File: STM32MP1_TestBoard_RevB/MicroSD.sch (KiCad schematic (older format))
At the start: 6 parts, among them J11 Micro_SD_Card

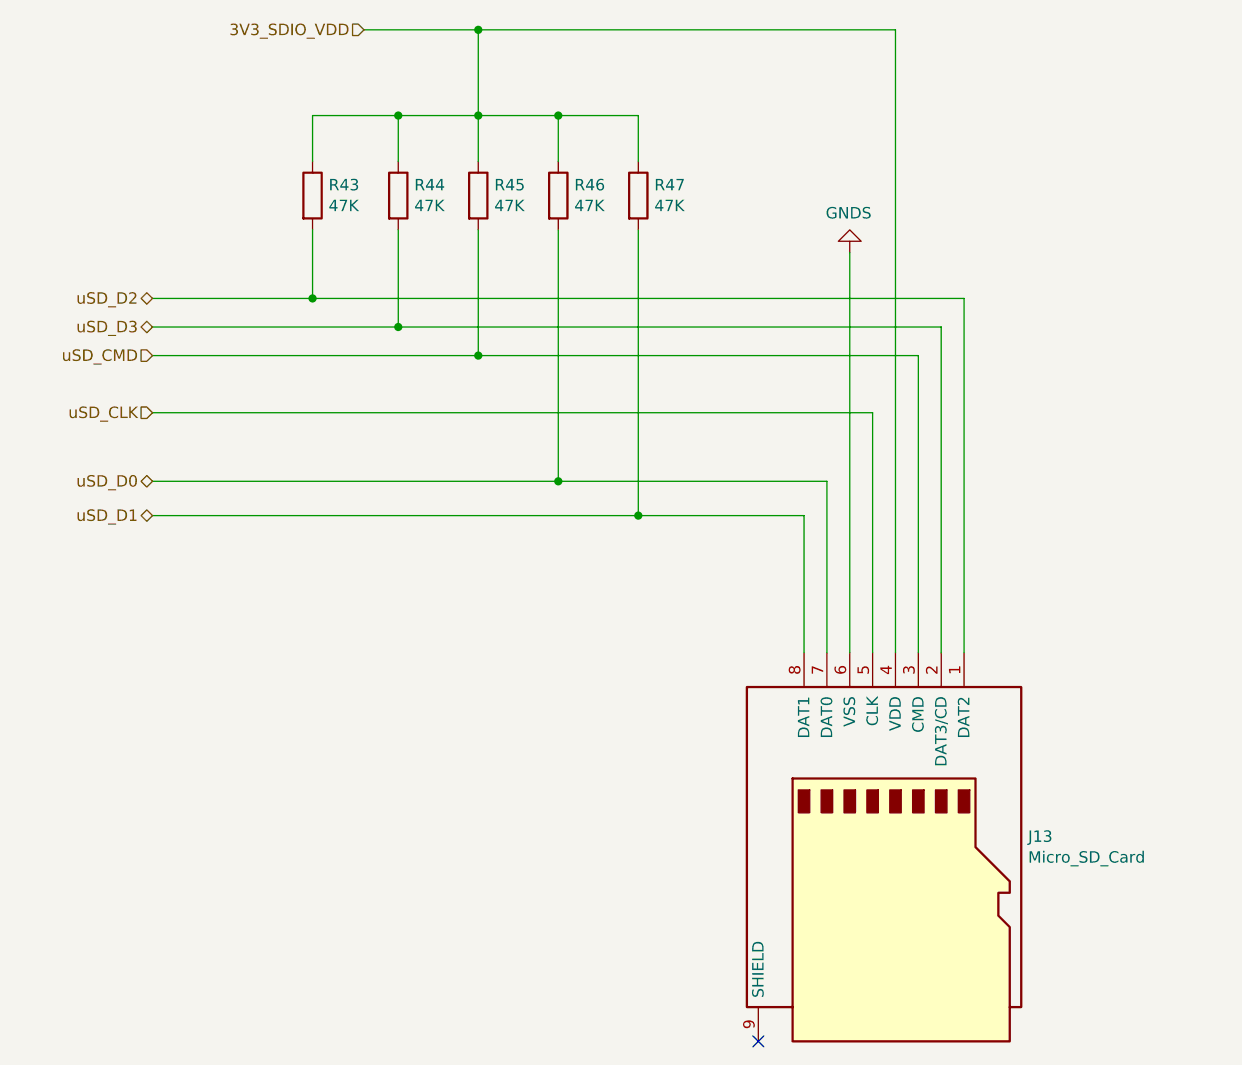
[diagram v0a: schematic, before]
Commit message: Updated design
- Added Crystal/Oscillators
- Replaced both SDMMC with single SDMMC w/ detect pin
- Added USB Type C for VIN
- Moved SWD pins
- Tidied up silk screen for pin headers J1, J2, J3, J4
- Moved DSI socket
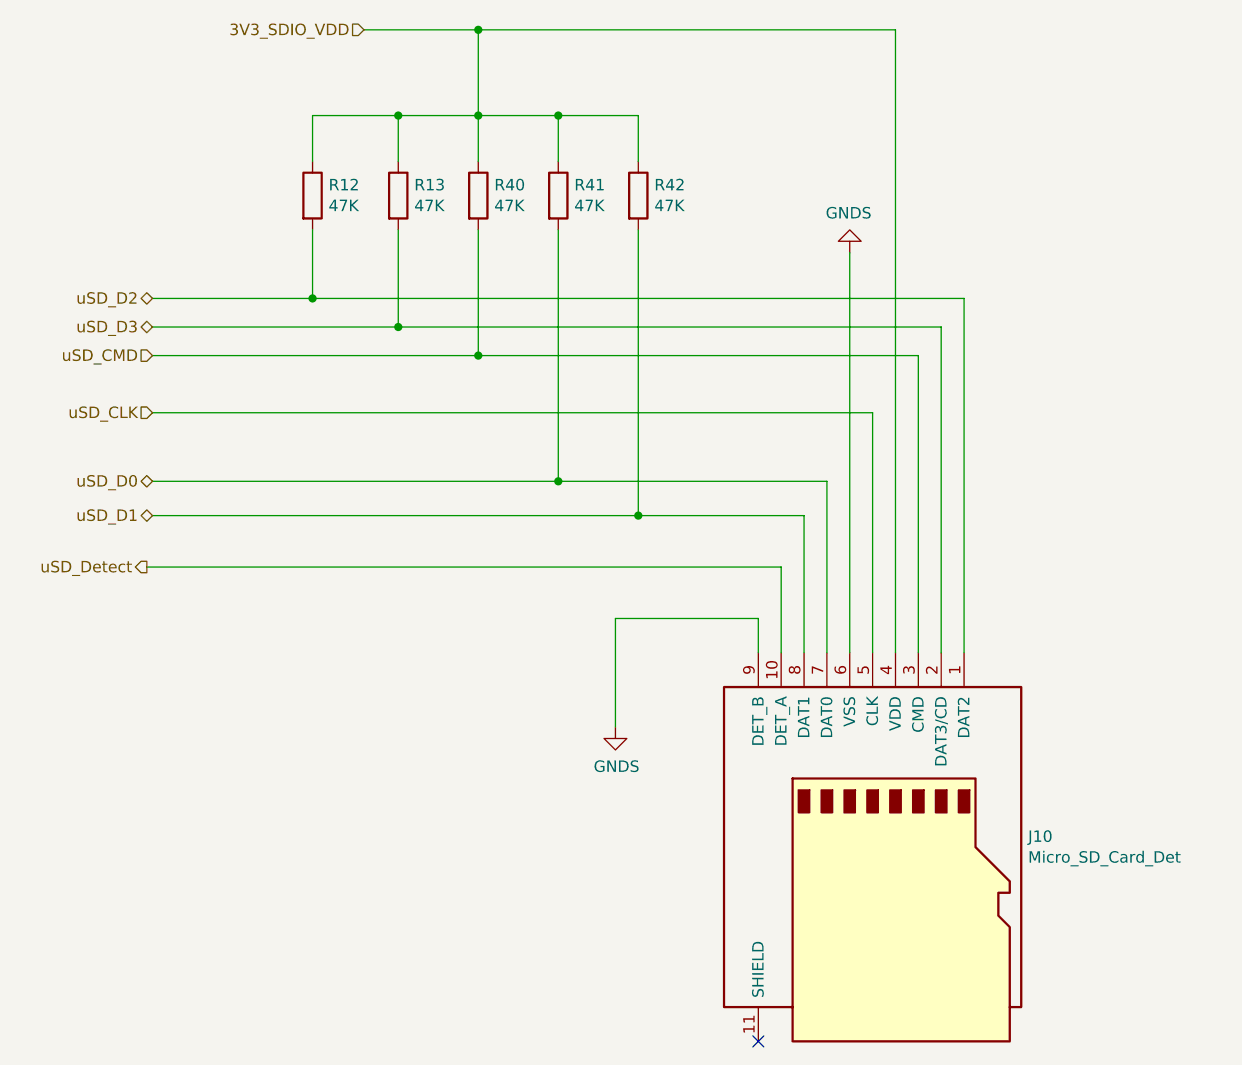
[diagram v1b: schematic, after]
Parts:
- removed J11: Micro_SD_Card, Molex_SDIO:Molex_SDIO_475710001, symbol Connector:Micro_SD_Card
- added J10: Micro_SD_Card_Det, Connector_Card:microSD_HC_Molex_104031-0811, symbol Connector:Micro_SD_Card_Det
- R40, R41, R42, R43, R44: LCSC (none) -> C25792
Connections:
- net 3V3_SDIO_VDD: now also J10.4 (VDD)
- net GNDS: now also J10.6 (VSS), J10.9 (DET_B)
- net uSD_CLK: now also J10.5 (CLK)
- net uSD_CMD: now also J10.3 (CMD)
- net uSD_D0: now also J10.7 (DAT0)
- net uSD_D1: now also J10.8 (DAT1)
- net uSD_D2: now also J10.1 (DAT2)
- net uSD_D3: now also J10.2 (DAT3/CD)
- new net uSD_Detect: J10.10 (DET_A)
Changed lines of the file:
@@
 $Descr A4 11693 8268
 encoding utf-8
-Sheet 10 10
+Sheet 8 9
 Title ""
 Date ""
@@
 AR Path="/6097C138/6099897C/5FB10A8F" Ref="#PWR045"  Part="1"
 AR Path="/6097C138/60E05EB1/5FB10A8F" Ref="#PWR0101"  Part="1"
-F 0 "#PWR0101" H 6900 1725 50  0001 C CNN
+F 0 "#PWR027" H 6900 1725 50  0001 C CNN
 F 1 "GNDS" H 6905 1802 50  0000 C CNN
 F 2 "" H 6900 1975 50  0001 C CNN
@@
 AR Path="/6097C138/6099897C/5FB12D8F" Ref="R43"  Part="1"
 AR Path="/6097C138/60E05EB1/5FB12D8F" Ref="R43"  Part="1"
-F 0 "R43" H 4620 1771 50  0000 L CNN
+F 0 "R12" H 4620 1771 50  0000 L CNN
 F 1 "47K" H 4620 1680 50  0000 L CNN
 F 2 "Resistor_SMD:R_0402_1005Metric_Pad0.72x0.64mm_HandSolder" V 4480 1725 50  0001 C CNN
@@
 F 4 "~" H 4550 1725 50  0001 C CNN "Mfr"
 F 5 "~" H 4550 1725 50  0001 C CNN "PartNo"
+F 6 "C25792" H 4550 1725 50  0001 C CNN "LCSC"
 	1    4550 1725
 	1    0    0    -1
@@
 AR Path="/6097C138/6099897C/5FB155D6" Ref="R44"  Part="1"
 AR Path="/6097C138/60E05EB1/5FB155D6" Ref="R44"  Part="1"
-F 0 "R44" H 4995 1771 50  0000 L CNN
+F 0 "R13" H 4995 1771 50  0000 L CNN
 F 1 "47K" H 4995 1680 50  0000 L CNN
 F 2 "Resistor_SMD:R_0402_1005Metric_Pad0.72x0.64mm_HandSolder" V 4855 1725 50  0001 C CNN
@@
 F 4 "~" H 4925 1725 50  0001 C CNN "Mfr"
 F 5 "~" H 4925 1725 50  0001 C CNN "PartNo"
+F 6 "C25792" H 4925 1725 50  0001 C CNN "LCSC"
 	1    4925 1725
 	1    0    0    -1
@@
 AR Path="/6097C138/6099897C/5FB158C2" Ref="R45"  Part="1"
 AR Path="/6097C138/60E05EB1/5FB158C2" Ref="R45"  Part="1"
-F 0 "R45" H 5345 1771 50  0000 L CNN
+F 0 "R40" H 5345 1771 50  0000 L CNN
 F 1 "47K" H 5345 1680 50  0000 L CNN
 F 2 "Resistor_SMD:R_0402_1005Metric_Pad0.72x0.64mm_HandSolder" V 5205 1725 50  0001 C CNN
@@
 F 4 "~" H 5275 1725 50  0001 C CNN "Mfr"
 F 5 "~" H 5275 1725 50  0001 C CNN "PartNo"
+F 6 "C25792" H 5275 1725 50  0001 C CNN "LCSC"
 	1    5275 1725
 	1    0    0    -1
@@
 AR Path="/6097C138/6099897C/5FB15A9B" Ref="R46"  Part="1"
 AR Path="/6097C138/60E05EB1/5FB15A9B" Ref="R46"  Part="1"
-F 0 "R46" H 5695 1771 50  0000 L CNN
+F 0 "R41" H 5695 1771 50  0000 L CNN
 F 1 "47K" H 5695 1680 50  0000 L CNN
 F 2 "Resistor_SMD:R_0402_1005Metric_Pad0.72x0.64mm_HandSolder" V 5555 1725 50  0001 C CNN
@@
 F 4 "~" H 5625 1725 50  0001 C CNN "Mfr"
 F 5 "~" H 5625 1725 50  0001 C CNN "PartNo"
+F 6 "C25792" H 5625 1725 50  0001 C CNN "LCSC"
 	1    5625 1725
 	1    0    0    -1
@@
 AR Path="/6097C138/6099897C/5FB15D60" Ref="R47"  Part="1"
 AR Path="/6097C138/60E05EB1/5FB15D60" Ref="R47"  Part="1"
-F 0 "R47" H 6045 1771 50  0000 L CNN
+F 0 "R42" H 6045 1771 50  0000 L CNN
 F 1 "47K" H 6045 1680 50  0000 L CNN
 F 2 "Resistor_SMD:R_0402_1005Metric_Pad0.72x0.64mm_HandSolder" V 5905 1725 50  0001 C CNN
@@
 F 4 "~" H 5975 1725 50  0001 C CNN "Mfr"
 F 5 "~" H 5975 1725 50  0001 C CNN "PartNo"
+F 6 "C25792" H 5975 1725 50  0001 C CNN "LCSC"
 	1    5975 1725
 	1    0    0    -1
@@
 Wire Wire Line
 	4925 1375 5275 1375
-$Comp
-L Connector:Micro_SD_Card J11
-U 1 1 5FA9DE35
-P 7100 4625
-AR Path="/60F0FA94/5FA9DE35" Ref="J11"  Part="1"
-AR Path="/60F1156A/5FA9DE35" Ref="J?"  Part="1"
-AR Path="/60F2D08D/5FA9DE35" Ref="J12"  Part="1"
-AR Path="/6097C138/60998974/5FA9DE35" Ref="J12"  Part="1"
-AR Path="/6097C138/6099897C/5FA9DE35" Ref="J13"  Part="1"
-AR Path="/6097C138/60E05EB1/5FA9DE35" Ref="J13"  Part="1"
-F 0 "J13" V 7004 5205 50  0000 L CNN
-F 1 "Micro_SD_Card" V 7095 5205 50  0000 L CNN
-F 2 "Molex_SDIO:Molex_SDIO_475710001" H 8250 4925 50  0001 C CNN
-F 3 "https://www.molex.com/molex/products/part-detail/memory_card_socket/0475710001" H 7100 4625 50  0001 C CNN
-F 4 "Molex" H 7100 4625 50  0001 C CNN "Mfr"
-F 5 "475710001" H 7100 4625 50  0001 C CNN "PartNo"
-	1    7100 4625
-	0    1    1    0
-$EndComp
 NoConn ~ 6500 5425
 Text HLabel 4775 1000 0    50   Input ~ 0
@@
 	7100 1000 7100 3725
 Connection ~ 5275 1000
+$Comp
+L Connector:Micro_SD_Card_Det J10
+U 1 1 605F163E
+P 7000 4625
+AR Path="/6097C138/60998974/605F163E" Ref="J10"  Part="1"
+AR Path="/6097C138/60E05EB1/605F163E" Ref="J?"  Part="1"
+F 0 "J10" V 6904 5305 50  0000 L CNN
+F 1 "Micro_SD_Card_Det" V 6995 5305 50  0000 L CNN
+F 2 "Connector_Card:microSD_HC_Molex_104031-0811" H 9050 5325 50  0001 C CNN
+F 3 "https://www.molex.com/webdocs/datasheets/pdf/en-us/1040310811_MEMORY_CARD_SOCKET.pdf" H 7000 4725 50  0001 C CNN
+	1    7000 4625
+	0    1    1    0
+$EndComp
+Wire Wire Line
+	6600 3725 6600 3350
+Wire Wire Line
+	6600 3350 3825 3350
+Text HLabel 3825 3350 0    50   Output ~ 0
+uSD_Detect
+Wire Wire Line
+	6500 3725 6500 3575
+Wire Wire Line
+	6500 3575 5875 3575
+Wire Wire Line
+	5875 3575 5875 4050
+$Comp
+L power:GNDS #PWR014
+U 1 1 605FE4FD
+P 5875 4050
+F 0 "#PWR014" H 5875 3800 50  0001 C CNN
+F 1 "GNDS" H 5880 3877 50  0000 C CNN
+F 2 "" H 5875 4050 50  0001 C CNN
+F 3 "" H 5875 4050 50  0001 C CNN
+	1    5875 4050
+	1    0    0    -1
+$EndComp
 $EndSCHEMATC

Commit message: completed revb layout
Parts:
- J10: Mfr (none) -> Molex; Mouser (none) -> 538-104031-0811; PartNo (none) -> 104031-0811
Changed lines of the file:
@@
 F 5 "~" H 4550 1725 50  0001 C CNN "PartNo"
 F 6 "C25792" H 4550 1725 50  0001 C CNN "LCSC"
+F 7 "~" H 4550 1725 50  0001 C CNN "Comment"
+F 8 "~" H 4550 1725 50  0001 C CNN "Mouser"
 	1    4550 1725
 	1    0    0    -1
@@
 F 5 "~" H 4925 1725 50  0001 C CNN "PartNo"
 F 6 "C25792" H 4925 1725 50  0001 C CNN "LCSC"
+F 7 "~" H 4925 1725 50  0001 C CNN "Comment"
+F 8 "~" H 4925 1725 50  0001 C CNN "Mouser"
 	1    4925 1725
 	1    0    0    -1
@@
 F 5 "~" H 5275 1725 50  0001 C CNN "PartNo"
 F 6 "C25792" H 5275 1725 50  0001 C CNN "LCSC"
+F 7 "~" H 5275 1725 50  0001 C CNN "Comment"
+F 8 "~" H 5275 1725 50  0001 C CNN "Mouser"
 	1    5275 1725
 	1    0    0    -1
@@
 F 5 "~" H 5625 1725 50  0001 C CNN "PartNo"
 F 6 "C25792" H 5625 1725 50  0001 C CNN "LCSC"
+F 7 "~" H 5625 1725 50  0001 C CNN "Comment"
+F 8 "~" H 5625 1725 50  0001 C CNN "Mouser"
 	1    5625 1725
 	1    0    0    -1
@@
 F 5 "~" H 5975 1725 50  0001 C CNN "PartNo"
 F 6 "C25792" H 5975 1725 50  0001 C CNN "LCSC"
+F 7 "~" H 5975 1725 50  0001 C CNN "Comment"
+F 8 "~" H 5975 1725 50  0001 C CNN "Mouser"
 	1    5975 1725
 	1    0    0    -1
@@
 F 2 "Connector_Card:microSD_HC_Molex_104031-0811" H 9050 5325 50  0001 C CNN
 F 3 "https://www.molex.com/webdocs/datasheets/pdf/en-us/1040310811_MEMORY_CARD_SOCKET.pdf" H 7000 4725 50  0001 C CNN
+F 4 "~" H 7000 4625 50  0001 C CNN "Comment"
+F 5 "~" H 7000 4625 50  0001 C CNN "LCSC"
+F 6 "Molex" H 7000 4625 50  0001 C CNN "Mfr"
+F 7 "538-104031-0811 " H 7000 4625 50  0001 C CNN "Mouser"
+F 8 "104031-0811 " H 7000 4625 50  0001 C CNN "PartNo"
 	1    7000 4625
 	0    1    1    0
